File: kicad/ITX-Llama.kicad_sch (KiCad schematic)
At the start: 422 parts, among them J1 ATX_POWER, J10 SATA, J11 SPEAKER, J12 MSD, J13 MT32-PI-GND, J14 AUDIO, J15 KBC, J16 KBD, J17 USB_ETH, J18 USB_HID, J19 HID_POWER, J2 MICRO_SD, J20 FAN1, J21 FAN2, J22 GAMEPORT, J23 WAVETABLE, J24 PI_ZERO2, J26 LEFT, J27 RIGHT, J28 COM2_TTL, J29 PI_2/3/4, J3 FRONT_PANEL, J30 FAN3, J31 FAN1_VDD, J32 FAN2_VDD, J33 FAN3_VDD, J34 CD_IN, J35 D1_MINI, J36 ESP_POWER, J38 J_TOSLINK_ZGY133T10, J39 LINE_L, J4 PS/2, J40 LINE_R, J41 EXT_SYNTH, J42 MT32-PI, J43 I2C, J46 RP_DEBUG, J5 AGP_3.3V, J6 CLICK_VOL, J7 MSC, J8 COM1, J9 INT_SPKR_VOL, P1 P_SOM-128-EX, Q1 NPN, Q10 Q_NMOS_GDS, Q11 Q_NMOS_GDS, Q2 NPN, Q3 NPN, Q4 NPN, Q5 NPN, Q6 NPN, Q7 NPN, Q8 Q_NMOS_GDS, Q9 Q_NMOS_GDS, SW1 CH559_PRG, SW1 POWER, SW2 RESET, T1 Pulse_H1102NL, U1 MAX16054, U10 U_MIC5219-3.3YM5, U11 EMC2303, U12 PCM5102A, U13 U_MIC5219-3.3YM5, U14 U_MIC5219-3.3YM5, U15 W25Q32JVSS, U16 U_74LVC1G126, U17 U_RP2040, U2 U_74LVC1G04, U3 U_CS4237B-KQ, U4 GD75232, U5 U_MC33078, U6 PI7C9X118SL, U7 AP7165, U8 U_MIC5219-3.3YM5, U9 U_ATTINY84A, X1 16.9344MHz, X2 12MHz

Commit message: Fix 'mono' sound issue when inserting IO Panel cables
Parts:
- removed J13: MT32-PI-GND, llama_shared:P_CONN_01X05, symbol llama_shared:P_MT32PI_GND
- removed LOGO2: RD_Logo, tinyllama:LOGO_retrodreams, symbol llama_shared:Llama_logo
- removed R122, R123: 27, llama_shared:R_0402_1005Metric, symbol llama_shared:R
- added FB8, FB9: 70Ω@100MHz, llama_shared:R_0603_1608Metric, symbol llama_shared:FB
- added J25: POWER, llama_shared:P_CONN_01X03, symbol Connector_Generic:Conn_01x03
- BT1: symbol llama_shared:BT -> tinyllama_shared:BT
- C27: LCSC C140782 -> (none)
- J1: LCSC C114088 -> C114125
- J42: value MT32-PI -> PI_I2C; footprint llama_shared:P_CONN_01X09 -> llama_shared:P_CONN_01X04; symbol llama_shared:P_MT32PI -> llama_shared:P_091OLED
- LOGO1: footprint llama_shared:LOGO_llama -> llama_shared:LLAMA_LOGO
- Q10, Q11, Q8, Q9: LCSC C5224263 -> C255592
- U3: LCSC C9900149464 -> (none)
- renumbered C1 to C48, C1 to C49, C1 to C50, C1 to C80, C1 to C81, C1 to C82, C1 to C83, R1 to R15, R2 to R16, R3 to R66, R4 to R67, SW1 to SW3
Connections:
- net UH2+ is gone; now on net USBHID2+: U17.36 (GPIO24)
- net UH2- is gone; now on net USBHID2-: U17.37 (GPIO25)
- net +3.3V: now also FB8.1, FB9.1; no longer C129.2, C130.2, C131.2, C159.1, C162.2, C164.2, C165.2, C166.2, C167.1, C168.1, C169.1, C170.1, C173.1, C38.2, C39.2, C40.2, C41.2, C42.2, C43.1, C44.1, C45.1, C46.1, C47.1, C53.1, C54.2, C56.2, C57.2, C58.2, C59.2, C60.2, C61.1, C62.1, C63.2, J5.A16 (VCC_3.3V), J5.A28 (VCC_3.3V), J5.A34 (Vddq3.3), J5.A40 (Vddq3.3), J5.A45 (VCC_3.3V), J5.A52 (Vddq3.3), J5.A58 (Vddq3.3), J5.A64 (Vddq3.3), J5.A9 (VCC_3.3V), J5.B16 (VCC_3.3V), J5.B28 (VCC_3.3V), J5.B34 (Vddq3.3), J5.B40 (Vddq3.3), J5.B45 (VCC_3.3V), J5.B47 (Vddq3.3), J5.B52 (Vddq3.3), J5.B58 (Vddq3.3), J5.B64 (Vddq3.3), J5.B9 (VCC_3.3V), R23.1, R26.1, R29.1, R30.1, R31.1, R32.1, R35.1, R41.1, R46.1, R47.1, R48.1, R49.1, R50.1
- net GND: now also J42.1 (GND); no longer J17.S (Shield), J42.4 (GND)
- net LIN: no longer J14.11
- net LMIC: no longer J14.2
- net LOUT: no longer J14.6
- net PI_SCL: now also J42.3 (SCL); no longer J42.2 (SCL)
- net PI_SDA: now also J42.4 (SDA); no longer J42.1 (SDA)
- net RIN: no longer J14.12
- net RMIC: no longer J14.4
- net ROUT: no longer J14.8
- net VCC: now also J25.2 (Pin_2); no longer C132.1, C135.1, J23.10 (VCC), J23.14 (VCC), J23.6 (VCC), J24.2 (5v), J24.4 (5v), J29.2 (5v), J29.4 (5v), U13.1 (IN), U13.3 (EN), U14.1 (IN), U14.3 (EN)
- removed net PI_3V3: J24.1 (3v3), J29.1 (3v3), J42.3 (3V3)
- removed net PI_BTN1: J24.11 (BCM17), J29.11 (BCM17), J42.5 (BTN1)
- removed net PI_BTN2: J24.13 (BCM27), J29.13 (BCM27), J42.6 (BTN2)
- removed net PI_BTN3: J24.15 (BCM22), J29.15 (BCM22), J42.7 (BTN3)
- removed net PI_BTN4: J24.16 (BCM23), J29.16 (BCM23), J42.8 (BTN4)
- removed net PI_BTN5: J24.7 (BCM4/GPCLK0), J29.7 (BCM4/GPCLK0), J42.9 (BTN5)
- new net VCC_3V3_AGP: C129.2, C130.2, C131.2, C159.1, C162.2, C164.2, C165.2, C166.2, C167.1, C168.1, C173.1, C61.1, C62.1, C63.2, FB8.2, J5.A16 (VCC_3.3V), J5.A28 (VCC_3.3V), J5.A45 (VCC_3.3V), J5.A9 (VCC_3.3V), J5.B16 (VCC_3.3V), J5.B28 (VCC_3.3V), J5.B45 (VCC_3.3V), J5.B9 (VCC_3.3V)
- new net VCC_PI: C132.1, C135.1, J24.2 (5v), J24.4 (5v), J25.3 (Pin_3), J29.2 (5v), J29.4 (5v), J42.2 (VCC), U13.1 (IN), U13.3 (EN), U14.1 (IN), U14.3 (EN)
- new net VCC_VIO_AGP: C169.1, C170.1, C38.2, C39.2, C40.2, C41.2, C42.2, C43.1, C44.1, C45.1, C46.1, C47.1, C53.1, C54.2, C56.2, C57.2, C58.2, C59.2, C60.2, FB9.2, J5.A34 (Vddq3.3), J5.A40 (Vddq3.3), J5.A52 (Vddq3.3), J5.A58 (Vddq3.3), J5.A64 (Vddq3.3), J5.B34 (Vddq3.3), J5.B40 (Vddq3.3), J5.B47 (Vddq3.3), J5.B52 (Vddq3.3), J5.B58 (Vddq3.3), J5.B64 (Vddq3.3), R23.1, R26.1, R29.1, R30.1, R31.1, R32.1, R35.1, R41.1, R46.1, R47.1, R48.1, R49.1, R50.1
- new net VCC_WT: J23.10 (VCC), J23.14 (VCC), J23.6 (VCC), J25.1 (Pin_1)
- no-connect marks 138 -> 157
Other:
- moved on the sheet: L4

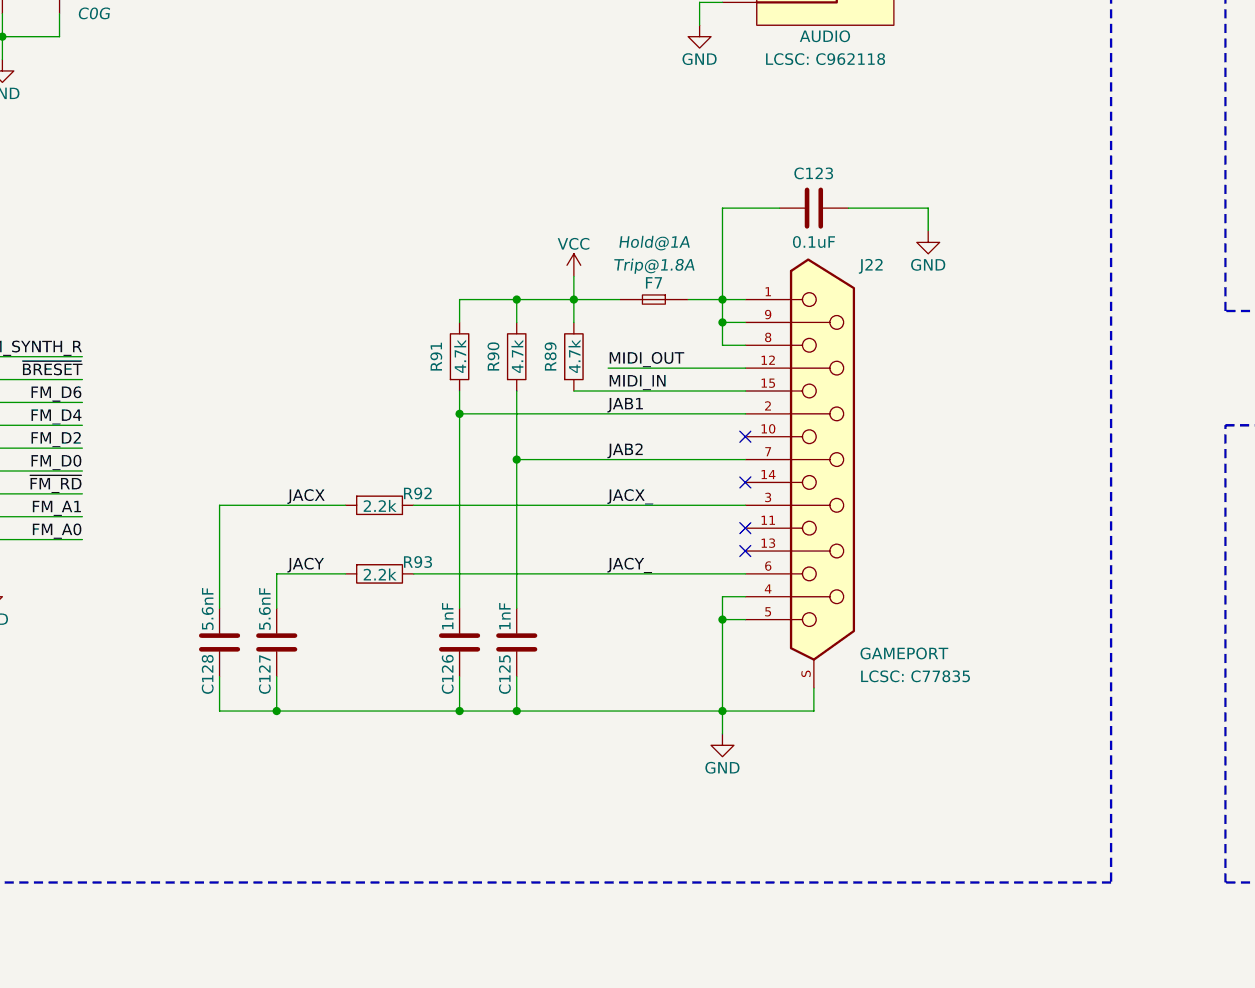
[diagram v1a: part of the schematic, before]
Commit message: Fix Gameport schematic, update Pi silkscreen
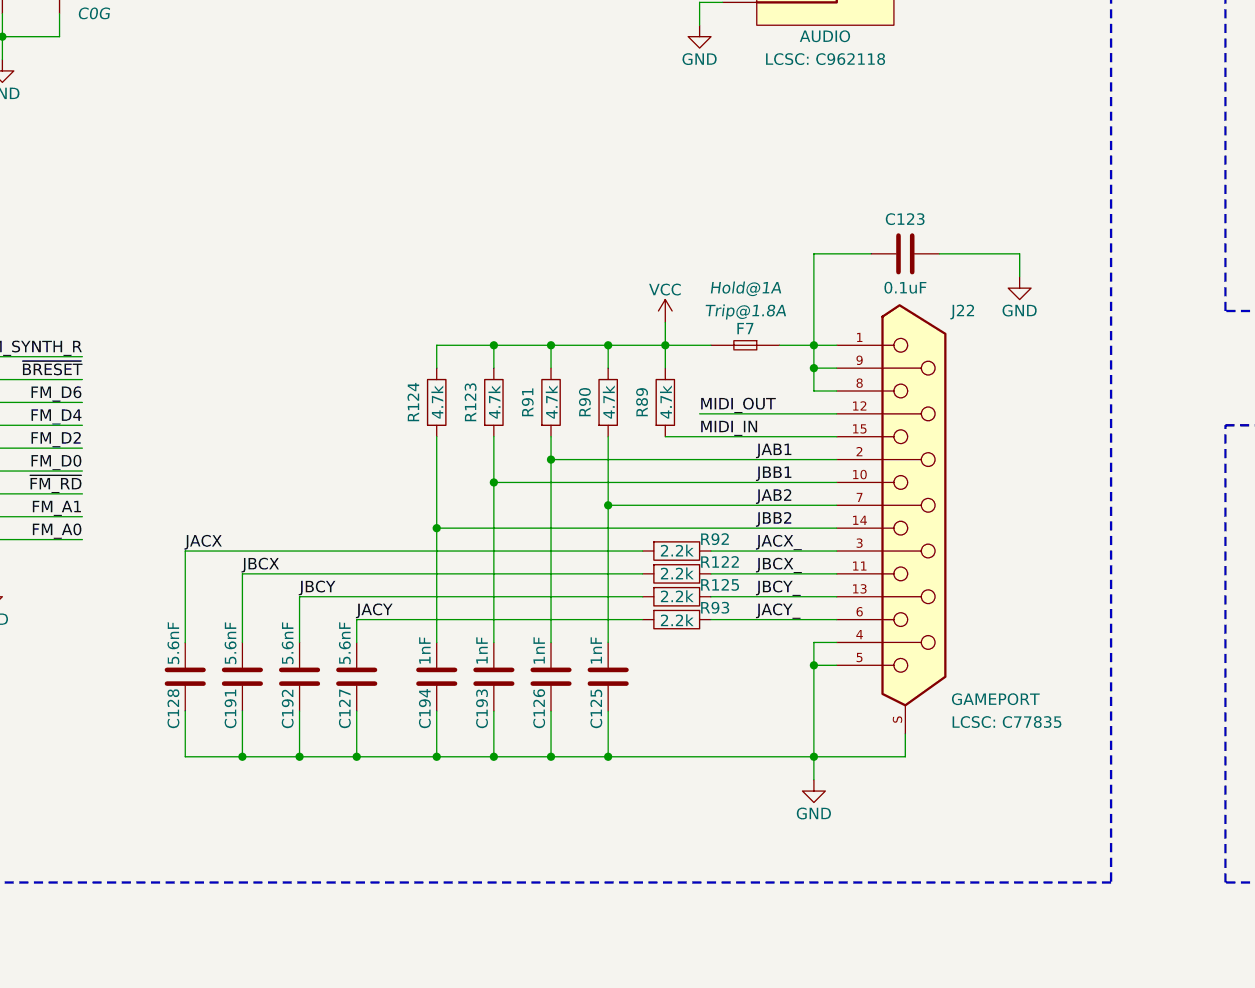
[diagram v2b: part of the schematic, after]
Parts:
- added C191, C192: 5.6nF, llama_shared:C_0402_1005Metric, symbol llama_shared:C
- added C193, C194: 1nF, llama_shared:C_0402_1005Metric, symbol llama_shared:C
- added R122, R125: 2.2k, llama_shared:R_0402_1005Metric, symbol llama_shared:R
- added R123, R124: 4.7k, llama_shared:R_0402_1005Metric, symbol llama_shared:R
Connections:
- net GND: now also C191.1, C192.1, C193.1, C194.1
- net VCC: now also R123.1, R124.1
- net JBB1: now reaches J22.10
- net JBB1: now also C193.2, R123.2
- net JBCX_: now reaches J22.11
- net JBCX_: now also R122.1
- net JBCY_: now reaches J22.13
- net JBCY_: now also R125.1
- net JBB2: now reaches J22.14
- net JBB2: now also C194.2, R124.2
- new net JBCX: C191.2, R122.2
- new net JBCY: C192.2, R125.2
- no-connect marks 157 -> 153
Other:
- moved on the sheet: C123, C125, C126, C127, C128, F7, J22, R89, R90, R91, R92, R93

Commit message: WIP: Traced Gameport, added passives to PCB, fix labels
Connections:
- net JBB1: now also U3.69 (JBB1*/FSYNC)
- net JBB2: now also U3.62 (JBB2*/SCLK)
- net JBCY: now also U3.64 (JBCY*/SDIN)
- no-connect marks 153 -> 150
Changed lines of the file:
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@@
 	)
 	(no_connect
-		(at 76.2 396.24)
-	)
-	(no_connect
 		(at 223.52 99.06)
 	)
@@
 	)
 	(no_connect
-		(at 71.12 396.24)
-	)
-	(no_connect
 		(at 157.48 553.72)
 	)
@@
 	)
 	(no_connect
-		(at 83.82 396.24)
-	)
-	(no_connect
 		(at 259.08 99.06)
 	)
@@
 	(wire
 		(pts
+			(xy 83.82 396.24) (xy 83.82 407.67)
+		)
+		(stroke
+			(width 0)
+			(type default)
+		)
+	)
+	(wire
+		(pts
 			(xy 816.61 107.95) (xy 822.96 107.95)
 		)
@@
 	(wire
 		(pts
+			(xy 76.2 396.24) (xy 76.2 407.67)
+		)
+		(stroke
+			(width 0)
+			(type default)
+		)
+	)
+	(wire
+		(pts
 			(xy 523.24 233.68) (xy 520.7 233.68)
 		)
@@
 	(wire
 		(pts
+			(xy 71.12 396.24) (xy 71.12 407.67)
+		)
+		(stroke
+			(width 0)
+			(type default)
+		)
+	)
+	(wire
+		(pts
 			(xy 402.59 96.52) (xy 414.02 96.52)
 		)
@@
 		)
 	)
+	(label "JBCY"
+		(at 76.2 407.67 90)
+		(effects
+			(font
+				(size 1.27 1.27)
+			)
+			(justify left bottom)
+		)
+	)
 	(label "PWM_HDD"
 		(at 694.69 623.57 180)
@@
 		)
 	)
+	(label "JBB1"
+		(at 83.82 407.67 90)
+		(effects
+			(font
+				(size 1.27 1.27)
+			)
+			(justify left bottom)
+		)
+	)
 	(label "AUDIO_L_WT"
 		(at 86.36 576.58 180)
@@
 		)
 	)
+	(label "JBB2"
+		(at 71.12 407.67 90)
+		(effects
+			(font
+				(size 1.27 1.27)
+			)
+			(justify left bottom)
+		)
+	)
 	(label "X_SD_DAT0"
 		(at 671.83 518.16 0)
@@
 			(font
 				(size 1.27 1.27)
+				(color 255 35 67 1)
 			)
 			(justify left bottom)
@@
 			)
 		)
-		(property "Datasheet" ""
+		(property "Datasheet" "~"
 			(at 245.11 440.69 0)
 			(effects
@@
 			)
 		)
-		(property "Description" ""
+		(property "Description" "15-pin female receptacle socket D-SUB connector (low-density/2 columns)"
 			(at 245.11 440.69 0)
 			(effects
@@
 					(size 1.27 1.27)
 				)
+				(hide yes)
 			)
 		)

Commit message: WIP: Latest tweaks to the schematic to align with PCB
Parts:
- renumbered R123 to R124, R122 to R126, R124 to R127
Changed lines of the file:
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@@
 		(on_board yes)
 		(dnp no)
-		(property "Reference" "R123"
+		(property "Reference" "R124"
 			(at 195.58 429.26 90)
 			(effects
@@
 			(project "ITX-Llama"
 				(path "/791931dd-db1e-41b7-962f-d560e0c7be07"
-					(reference "R123")
+					(reference "R124")
 					(unit 1)
 				)
@@
 		(on_board yes)
 		(dnp no)
-		(property "Reference" "R122"
+		(property "Reference" "R126"
 			(at 220.98 447.04 90)
 			(effects
@@
 			(project "ITX-Llama"
 				(path "/791931dd-db1e-41b7-962f-d560e0c7be07"
-					(reference "R122")
+					(reference "R126")
 					(unit 1)
 				)
@@
 		(on_board yes)
 		(dnp no)
-		(property "Reference" "R124"
+		(property "Reference" "R127"
 			(at 189.23 429.26 90)
 			(effects
@@
 			(project "ITX-Llama"
 				(path "/791931dd-db1e-41b7-962f-d560e0c7be07"
-					(reference "R124")
+					(reference "R127")
 					(unit 1)
 				)
